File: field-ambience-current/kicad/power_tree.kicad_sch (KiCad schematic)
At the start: 9 parts, among them J1 USB_C_Receptacle (TYPE-C-31-M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

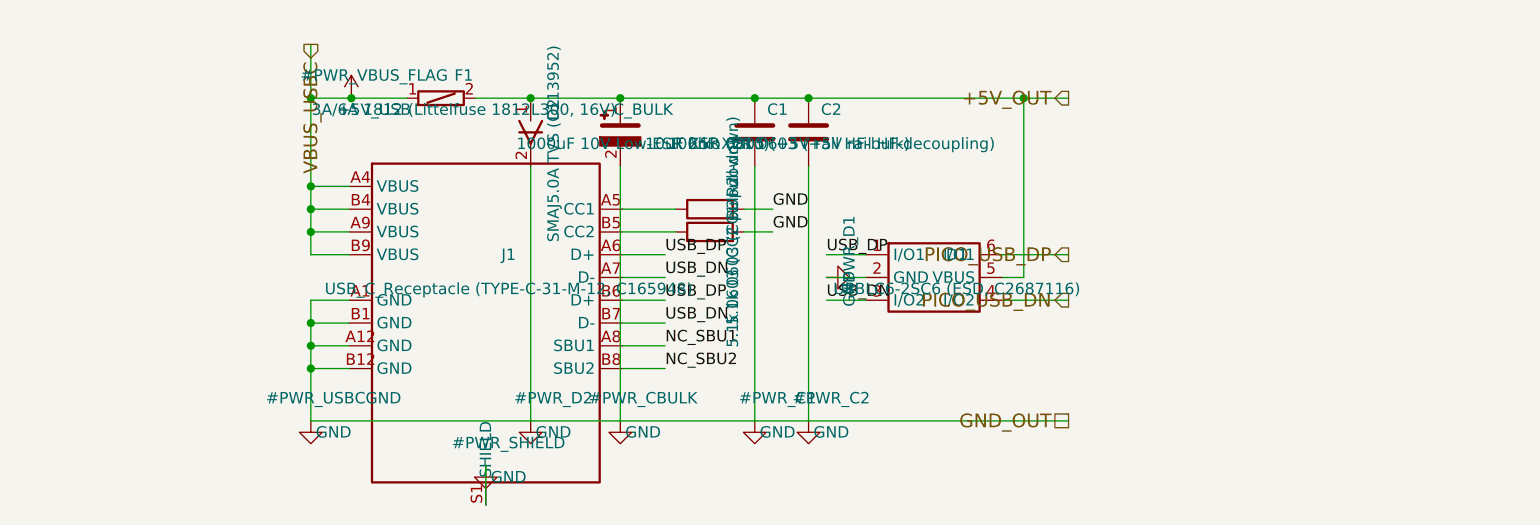
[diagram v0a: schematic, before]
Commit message: pcb(r18.5): Schematic-Migration Phase 3 — STM32H743 + LCD im Generator, Repo-Audit-Fixes
KERN: generate_kicad_project.py erzeugt jetzt die H7-Architektur.

NEU stm32h743.kicad_sch (ersetzt pico.kicad_sch -> kicad/legacy_pico2/):
- 100-Pin-Symbol 1:1 aus offizieller KiCad-Lib (MCU_ST_STM32H7),
  doppelt verifiziert gegen SPEC v0.7 §5 / DS12110 Rev 5 Table 8 —
  alle 52 belegten Zuordnungen identisch (zwei unabhängige Quellen)
- alle SPEC-§5-Netze verdrahtet, 48 Reserve-GPIOs no_connect
- Support: HSE Y1 ABLS-8.000MHZ-B4-T (C596838) + 2x22pF, VCAP 2x2.2uF
  (DS12110 Tab.24), 5x(4.7uF+100nF) VDD-Bank, VDDA-Ferrit C84094 +
  1uF+100nF, BOOT0-PD 10k, NRST-PU 10k+100nF, SWD-J4 (PA13/PA14/GND),
  BAT-Teiler 100k/100k+10nF an PA3, Status-LED PD8, USB-FS PA11/PA12
  (USBLC6-ESD bleibt davor), MIDI_TX-Netz (PD5)

NEU lcd.kicad_sch (ersetzt oled.kicad_sch -> legacy): 8-Pin-ST7789
per SPEC §6 + C6b/C6c + Backlight: PCA9685-Kanal-12 -> LCD_BLK_PWM ->
2N7002 Low-Side + 100k-PD. Netze OLED_* -> LCD_*.

power_tree: U5 AP7361A-33 LDO (+5V->+3V3) + Cin 1uF/Cout 2.2uF +
EN->IN. Pico-SMPS entfällt. PICO_USB_* -> USB_DM/USB_DP.

mcp: GPB5 = VOL_SW (SPEC §5.4 — lag bis r17 entgegen der SPEC am
Pico-GPIO), PCA-Kanal 12 = LCD_BLK_PWM. Root-Brücken umgebaut,
kicad_pro-Sheetliste: Battery ergänzt (fehlte).

AUDIT-FINDINGS (verifiziert, nicht aus dem Alt-Audit übernommen):
- F-6 NEU 🔴: SPEC-§4-U5-LCSC C156144 ist ein 910R-WIDERSTAND
  (LCSC-Web verifiziert) — hätte bei JLC einen R als LDO bestückt.
  SPEC korrigiert (Kandidat C150719), Symbol trägt TBD-VERIFY.
- B-LDO 🔴: AP7361A-SOT-89-5-Pinout-Annahme (1=ADJ/NC,2=OUT,3=IN,
  4=GND,5=EN aus AP7361-DS33626-Lesart; A-Datasheet war HTTP 403) —
  als PIN_VERIFY am Symbol + PCB_LAYOUT_STATUS dokumentiert.
- B-SW12 🔴: SW6-10 (HX 12x12) auf ~6mm-TL3342-Pattern — als
  FP_MISMATCH-Property an allen 5 Symbolen markiert.
- F-2-Teilfix: Encoder-MPN -> EC11J1525402, Bourns-PEC11R-PDF nach
  datasheets/legacy/ (falsches Teil); ALPS-Drawing offen.
- F-1: T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
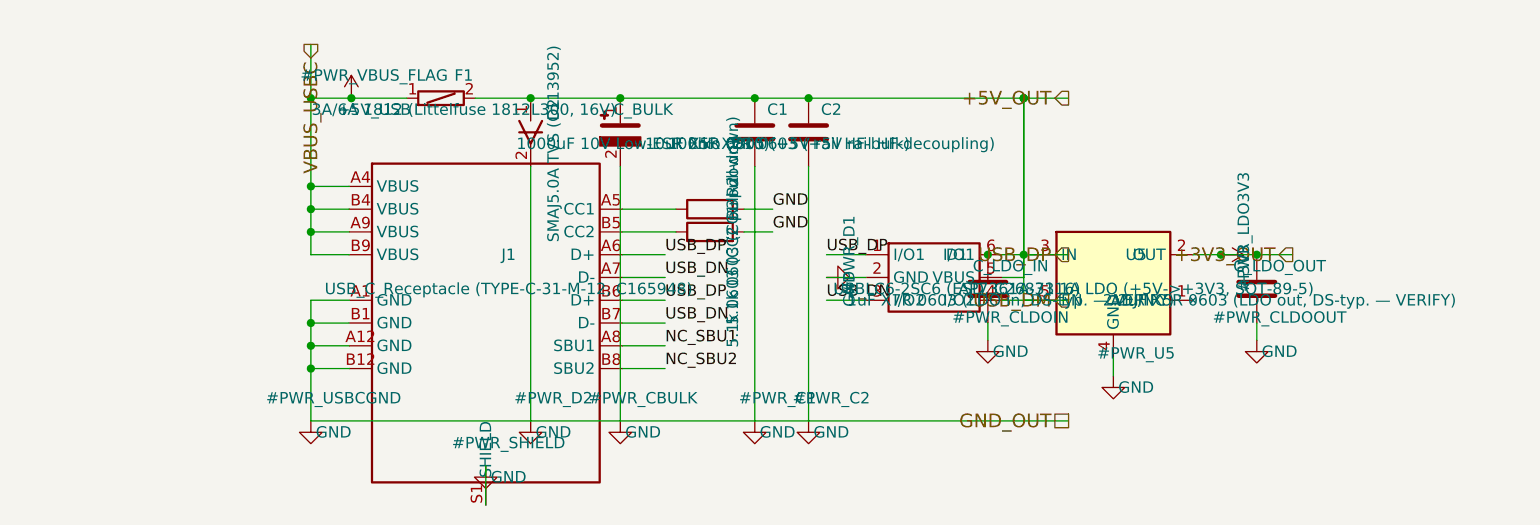
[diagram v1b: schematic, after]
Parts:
- added C_LDO_IN: 1uF X7R 0603 (LDO in, DS-typ. — VERIFY), Capacitor_SMD:C_0603_1608Metric, symbol Device:C
- added C_LDO_OUT: 2.2uF X5R 0603 (LDO out, DS-typ. — VERIFY), Capacitor_SMD:C_0603_1608Metric, symbol Device:C
- added U5: AP7361A-33 1A LDO (+5V->+3V3, SOT-89-5), Package_TO_SOT_SMD:SOT-89-5, symbol Regulator_Linear:AP7361A
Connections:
- net PICO_USB_DN is gone; now on net +5V_OUT: D1.4 (I/O2)
- net PICO_USB_DP is gone; now on net +5V_OUT: D1.6 (I/O1)
- net USB_DP is gone; now on net +5V_OUT: D1.1 (I/O1), J1.A6 (D+), J1.B6 (D+)
- net +5V_OUT: now also U5.3 (IN), U5.5 (EN)
- net GND: now also C_LDO_IN.2, C_LDO_OUT.2, U5.4 (GND)
- new net +3V3: C_LDO_OUT.1, U5.2 (OUT)
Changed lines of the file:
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@@
       (project "field_ambience"
         (path "/8f124281-8f89-47ab-aa39-bcbf8f1e5e4d" (reference "#PWR_SHIELD") (unit 1)))))
+  (symbol (lib_id "Regulator_Linear:AP7361A") (at 120.0 80.0 0) (unit 1)
+    (in_bom yes) (on_board yes) (dnp no)
+      (property "Reference" "U5" (at 122.54 77.46 0)
+        (effects (font (size 1.27 1.27))))
+      (property "Value" "AP7361A-33 1A LDO (+5V->+3V3, SOT-89-5)" (at 122.54 81.27 0)
+        (effects (font (size 1.27 1.27))))
+      (property "Footprint" "Package_TO_SOT_SMD:SOT-89-5" (at 120.0 80.0 0)
+        (effects (font (size 1.27 1.27)) hide))
+      (property "Datasheet" "https://www.diodes.com/assets/Datasheets/AP7361.pdf" (at 120.0 80.0 0)
+        (effects (font (size 1.27 1.27)) hide))
+      (property "MPN" "AP7361A-33ER-13" (at 122.54 83.81 0)
+        (effects (font (size 1.27 1.27)) hide))
+      (property "LCSC" "TBD-VERIFY (C156144 in SPEC war FALSCH = 910R-Widerstand; Kandidat C150719 = AP7361-33E-13)" (at 122.54 85.08 0)
+        (effects (font (size 1.27 1.27)) hide))
+      (property "PIN_VERIFY" "B-LDO: SOT-89-5-Pinout (1=ADJ/NC,2=OUT,3=IN,4=GND,5=EN) gegen offizielles AP7361A-DS pruefen — IN/OUT-Tausch = totes Board" (at 122.54 86.35 0)
+        (effects (font (size 1.27 1.27)) hide))
+      (property "FP_VERIFY" "SOT-89-5-Footprint-Name + Land-Pattern in Phase-3-GUI pruefen" (at 122.54 87.62 0)
+        (effects (font (size 1.27 1.27)) hide))
+    (instances
+      (project "field_ambience"
+        (path "/8f124281-8f89-47ab-aa39-bcbf8f1e5e4d" (reference "U5") (unit 1)))))
+  (symbol (lib_id "Power:GND") (at 120.0 91.0 0) (unit 1)
+    (in_bom yes) (on_board yes) (dnp no)
+      (property "Reference" "#PWR_U5" (at 122.54 88.46 0)
+        (effects (font (size 1.27 1.27))))
+      (property "Value" "GND" (at 122.54 92.27 0)
+        (effects (font (size 1.27 1.27))))
+      (property "Footprint" "" (at 120.0 91.0 0)
+        (effects (font (size 1.27 1.27)) hide))
+      (property "Datasheet" "~" (at 120.0 91.0 0)
+        (effects (font (size 1.27 1.27)) hide))
+    (instances
+      (project "field_ambience"
+        (path "/8f124281-8f89-47ab-aa39-bcbf8f1e5e4d" (reference "#PWR_U5") (unit 1)))))
+  (symbol (lib_id "Device:C") (at 106 81.27 0) (unit 1)
+    (in_bom yes) (on_board yes) (dnp no)
+      (property "Reference" "C_LDO_IN" (at 108.54 78.72999999999999 0)
+        (effects (font (size 1.27 1.27))))
+      (property "Value" "1uF X7R 0603 (LDO in, DS-typ. — VERIFY)" (at 108.54 82.53999999999999 0)
+        (effects (font (size 1.27 1.27))))
+      (property "Footprint" "Capacitor_SMD:C_0603_1608Metric" (at 106 81.27 0)
+        (effects (font (size 1.27 1.27)) hide))
+      (property "Datasheet" "~" (at 106 81.27 0)
+        (effects (font (size 1.27 1.27)) hide))
+      (property "MPN" "CL10A105KB8NNNC" (at 108.54 85.08 0)
+        (effects (font (size 1.27 1.27)) hide))
+      (property "LCSC" "C15849" (at 108.54 86.35 0)
+        (effects (font (size 1.27 1.27)) hide))
+    (instances
+      (project "field_ambience"
+        (path "/8f124281-8f89-47ab-aa39-bcbf8f1e5e4d" (reference "C_LDO_IN") (unit 1)))))
+  (symbol (lib_id "Power:GND") (at 106 87.0 0) (unit 1)
+    (in_bom yes) (on_board yes) (dnp no)
+      (property "Reference" "#PWR_CLDOIN" (at 108.54 84.46 0)
+        (effects (font (size 1.27 1.27))))
+      (property "Value" "GND" (at 108.54 88.27 0)
+        (effects (font (size 1.27 1.27))))
+      (property "Footprint" "" (at 106 87.0 0)
+        (effects (font (size 1.27 1.27)) hide))
+      (property "Datasheet" "~" (at 106 87.0 0)
+        (effects (font (size 1.27 1.27)) hide))
+    (instances
+      (project "field_ambience"
+        (path "/8f124281-8f89-47ab-aa39-bcbf8f1e5e4d" (reference "#PWR_CLDOIN") (unit 1)))))
+  (symbol (lib_id "Power:+3V3") (at 132 77.46 270) (unit 1)
+    (in_bom yes) (on_board yes) (dnp no)
+      (property "Reference" "#PWR_LDO3V3" (at 134.54 74.91999999999999 0)
+        (effects (font (size 1.27 1.27))))
+      (property "Value" "+3V3" (at 134.54 78.72999999999999 0)
+        (effects (font (size 1.27 1.27))))
+      (property "Footprint" "" (at 132 77.46 0)
+        (effects (font (size 1.27 1.27)) hide))
+      (property "Datasheet" "~" (at 132 77.46 0)
+        (effects (font (size 1.27 1.27)) hide))
+    (instances
+      (project "field_ambience"
+        (path "/8f124281-8f89-47ab-aa39-bcbf8f1e5e4d" (reference "#PWR_LDO3V3") (unit 1)))))
+  (symbol (lib_id "Device:C") (at 136 81.27 0) (unit 1)
+    (in_bom yes) (on_board yes) (dnp no)
+      (property "Reference" "C_LDO_OUT" (at 138.54 78.72999999999999 0)
+        (effects (font (size 1.27 1.27))))
+      (property "Value" "2.2uF X5R 0603 (LDO out, DS-typ. — VERIFY)" (at 138.54 82.53999999999999 0)
+        (effects (font (size 1.27 1.27))))
+      (property "Footprint" "Capacitor_SMD:C_0603_1608Metric" (at 136 81.27 0)
+        (effects (font (size 1.27 1.27)) hide))
+      (property "Datasheet" "~" (at 136 81.27 0)
+        (effects (font (size 1.27 1.27)) hide))
+      (property "MPN" "TBD-VERIFY (2.2uF/10V X5R 0603)" (at 138.54 85.08 0)
+        (effects (font (size 1.27 1.27)) hide))
+      (property "LCSC" "TBD-VERIFY" (at 138.54 86.35 0)
+        (effects (font (size 1.27 1.27)) hide))
+    (instances
+      (project "field_ambience"
+        (path "/8f124281-8f89-47ab-aa39-bcbf8f1e5e4d" (reference "C_LDO_OUT") (unit 1)))))
+  (symbol (lib_id "Power:GND") (at 136 87.0 0) (unit 1)
+    (in_bom yes) (on_board yes) (dnp no)
+      (property "Reference" "#PWR_CLDOOUT" (at 138.54 84.46 0)
+        (effects (font (size 1.27 1.27))))
+      (property "Value" "GND" (at 138.54 88.27 0)
+        (effects (font (size 1.27 1.27))))
+      (property "Footprint" "" (at 136 87.0 0)
+        (effects (font (size 1.27 1.27)) hide))
+      (property "Datasheet" "~" (at 136 87.0 0)
+        (effects (font (size 1.27 1.27)) hide))
+    (instances
+      (project "field_ambience"
+        (path "/8f124281-8f89-47ab-aa39-bcbf8f1e5e4d" (reference "#PWR_CLDOOUT") (unit 1)))))
   (wire (pts (xy 34.76 69.84) (xy 30.48 69.84))
     (stroke (width 0) (type default))
@@
     (stroke (width 0) (type default))
 )
+  (wire (pts (xy 110 60.0) (xy 110 77.46))
+    (stroke (width 0) (type default))
+)
+  (wire (pts (xy 110 77.46) (xy 111.11 77.46))
+    (stroke (width 0) (type default))
+)
+  (wire (pts (xy 111.11 82.54) (xy 110 82.54))
+    (stroke (width 0) (type default))
+)
+  (wire (pts (xy 110 82.54) (xy 110 77.46))
+    (stroke (width 0) (type default))
+)
+  (wire (pts (xy 120.0 88.89) (xy 120.0 91.0))
+    (stroke (width 0) (type default))
+)
+  (wire (pts (xy 106 77.46) (xy 106 77.46))
+    (stroke (width 0) (type default))
+)
+  (wire (pts (xy 106 85.08) (xy 106 87.0))
+    (stroke (width 0) (type default))
+)
+  (wire (pts (xy 128.89 77.46) (xy 140 77.46))
+    (stroke (width 0) (type default))
+)
+  (wire (pts (xy 136 77.46) (xy 136 77.46))
+    (stroke (width 0) (type default))
+)
+  (wire (pts (xy 136 85.08) (xy 136 87.0))
+    (stroke (width 0) (type default))
+)
   (wire (pts (xy 110 60.0) (xy 115 60.0))
     (stroke (width 0) (type default))
@@
 )
   (junction (at 110 60.0) (diameter 0) (color 0 0 0 0)
+)
+  (junction (at 110 60.0) (diameter 0) (color 0 0 0 0)
+)
+  (junction (at 110 77.46) (diameter 0) (color 0 0 0 0)
+)
+  (junction (at 106 77.46) (diameter 0) (color 0 0 0 0)
+)
+  (junction (at 132 77.46) (diameter 0) (color 0 0 0 0)
+)
+  (junction (at 136 77.46) (diameter 0) (color 0 0 0 0)
 )
   (label "GND" (at 82 72.38 0) (fields_autoplaced)
@@
     (effects (font (size 1.524 1.524)) (justify right))
 )
-  (hierarchical_label "PICO_USB_DP" (shape output) (at 115 77.46 0)
+  (hierarchical_label "USB_DP" (shape output) (at 115 77.46 0)
     (effects (font (size 1.524 1.524)) (justify right))
 )
-  (hierarchical_label "PICO_USB_DN" (shape output) (at 115 82.54 0)
+  (hierarchical_label "USB_DM" (shape output) (at 115 82.54 0)
     (effects (font (size 1.524 1.524)) (justify right))
 )
+  (hierarchical_label "+3V3_OUT" (shape output) (at 140 77.46 180)
+    (effects (font (size 1.524 1.524)) (justify right))
+)
